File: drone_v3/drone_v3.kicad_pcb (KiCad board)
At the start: 2 copper layers, 47.5 x 47.5 mm, 94 parts, among them J1 USB_B_Micro, J14 Conn_01x02_Male, J19 Micro_SD_Card, J2 Conn_01x10_Female, J7 Conn_01x04_Male, J9 Conn_01x06_Male, Q1 2N3904, Q2 2N3904, U3 MPU-9250, U7 BMP388, U9 MCP1700-3302E_SOT23, Y1 Crystal_GND24

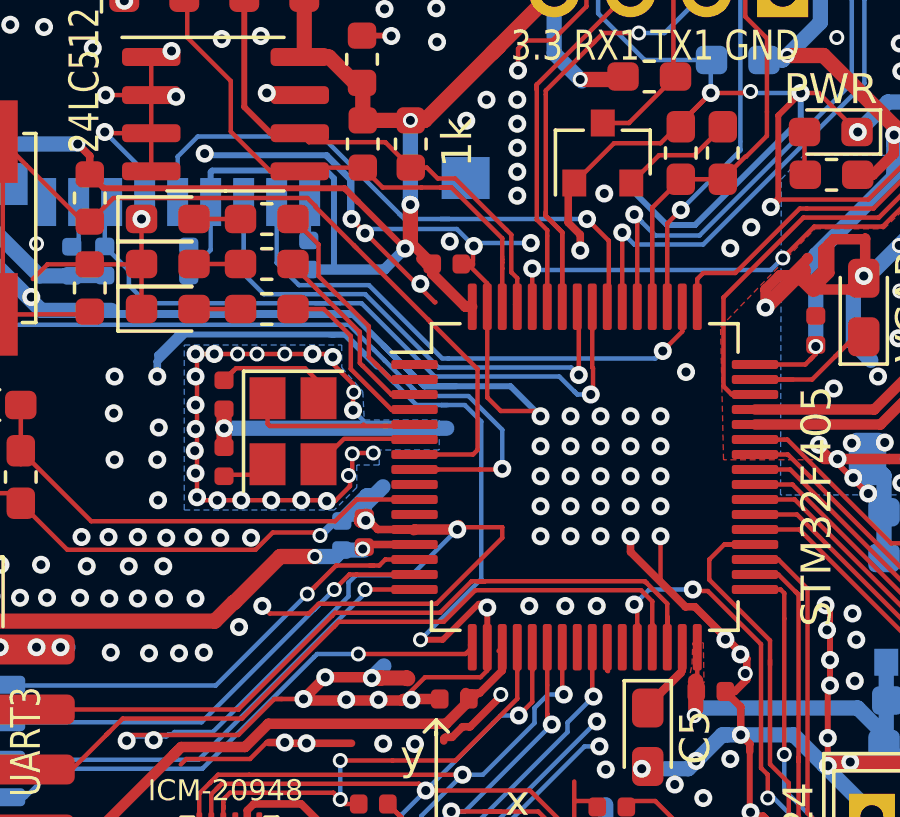
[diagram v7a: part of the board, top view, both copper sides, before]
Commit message: clearance to 0.2
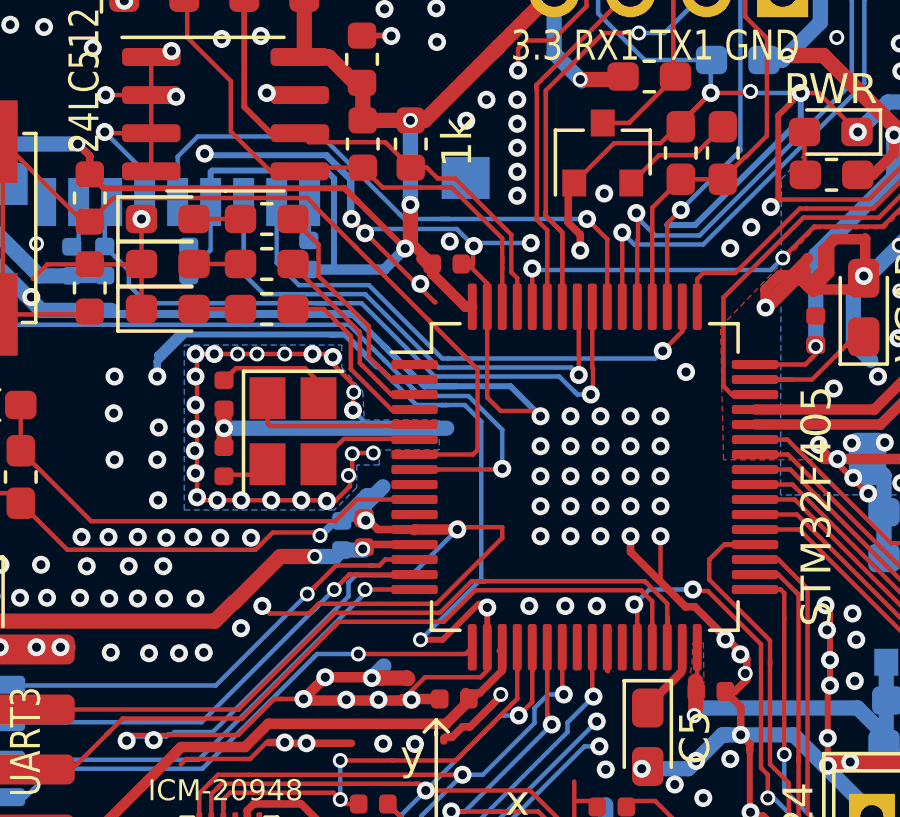
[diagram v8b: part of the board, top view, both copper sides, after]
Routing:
- net GND: track 657.6 -> 655.6 mm
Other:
- net class Default: clearance 0.15 -> 0.2
- rule trace_clearance: 0.15 -> 0.2
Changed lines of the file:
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@@
     (thickness 1.6)
     (drawings 10)
-    (tracks 1967)
+    (tracks 1968)
     (zones 0)
     (modules 94)
@@
     (user_trace_width 0.508)
     (user_trace_width 1.5)
-    (trace_clearance 0.15)
+    (trace_clearance 0.2)
     (zone_clearance 0.2)
     (zone_45_only no)
@@
   (net 103 PWR_IN)
   (net_class Default "This is the default net class."
-    (clearance 0.15)
+    (clearance 0.2)
     (trace_width 0.15)
     (via_dia 0.6)
@@
   (segment (start 128.125 124.65) (end 128.175 124.65) (width 0.15) (layer F.Cu) (net 1))
   (via (at 118.85 110.3) (size 0.6) (drill 0.3) (layers F.Cu B.Cu) (net 1))
-  (via (at 118.075 111) (size 0.6) (drill 0.3) (layers F.Cu B.Cu) (net 1))
+  (via (at 118.14 111.04) (size 0.6) (drill 0.3) (layers F.Cu B.Cu) (net 1))
   (segment (start 122.41651 97.73349) (end 122.275 97.875) (width 0.15) (layer B.Cu) (net 1))
   (segment (start 125.33349 97.73349) (end 122.41651 97.73349) (width 0.15) (layer B.Cu) (net 1))
@@
   (segment (start 129.45 98.45) (end 129.45 97.922816) (width 0.254) (layer F.Cu) (net 1))
   (segment (start 132.340003 97.600001) (end 133.274999 97.600001) (width 0.2) (layer B.Cu) (net 1))
-  (segment (start 130.940002 96.2) (end 132.340003 97.600001) (width 0.2) (layer B.Cu) (net 1))
   (segment (start 136.8 94.075) (end 136.8 93.2) (width 0.2) (layer B.Cu) (net 1))
   (segment (start 133.274999 97.600001) (end 136.8 94.075) (width 0.2) (layer B.Cu) (net 1))
@@
   (segment (start 144.268797 89.726201) (end 144.326201 89.726201) (width 0.15) (layer F.Cu) (net 31))
   (segment (start 141.44759 92.547408) (end 144.268797 89.726201) (width 0.15) (layer F.Cu) (net 31))
-  (segment (start 130.85 100.325) (end 130.85 97.85) (width 0.15) (layer F.Cu) (net 32))
   (segment (start 130.85 97.85) (end 130.85 97.85) (width 0.15) (layer F.Cu) (net 32))
   (via (at 130.85 97.85) (size 0.6) (drill 0.3) (layers F.Cu B.Cu) (net 32))
@@
   (segment (start 138.92 90.08) (end 141.58 87.42) (width 0.15) (layer B.Cu) (net 32))
   (segment (start 138.92 92.876998) (end 138.92 90.08) (width 0.15) (layer B.Cu) (net 32))
-  (segment (start 131.35 100.325) (end 131.35 97.35) (width 0.15) (layer F.Cu) (net 33))
-  (segment (start 131.35 97.35) (end 131.25 97.25) (width 0.15) (layer F.Cu) (net 33))
   (segment (start 131.25 97.25) (end 131.25 97.25) (width 0.15) (layer F.Cu) (net 33))
-  (via (at 131.25 97.25) (size 0.6) (drill 0.3) (layers F.Cu B.Cu) (net 33) (status 1000000))
+  (via (at 131.32 97.2) (size 0.6) (drill 0.3) (layers F.Cu B.Cu) (net 33))
   (segment (start 131.25 97.25) (end 131.5 97.5) (width 0.15) (layer B.Cu) (net 33))
   (segment (start 140.75 85.96) (end 140.75 87.825722) (width 0.15) (layer B.Cu) (net 33))
@@
   (segment (start 123.589088 97.4) (end 123.65 97.4) (width 0.15) (layer B.Cu) (net 50))
   (segment (start 124.8 97.4) (end 123.65 97.4) (width 0.15) (layer B.Cu) (net 50))
-  (segment (start 130.4 98.125) (end 129.675 97.4) (width 0.15) (layer F.Cu) (net 50))
   (segment (start 130.35 100.325) (end 130.4 100.275) (width 0.15) (layer F.Cu) (net 50))
-  (segment (start 130.4 100.275) (end 130.4 98.125) (width 0.15) (layer F.Cu) (net 50))
   (segment (start 129.2 97.4) (end 124.8 97.4) (width 0.15) (layer B.Cu) (net 50))
   (segment (start 129.675 97.4) (end 129.2 97.4) (width 0.15) (layer B.Cu) (net 50))
@@
   (segment (start 128.85 100.325) (end 128.85 97.85) (width 0.15) (layer F.Cu) (net 28))
   (segment (start 128.85 97.85) (end 128.3 97.3) (width 0.15) (layer F.Cu) (net 28))
+  (segment (start 130.85 100.325) (end 130.85 97.85) (width 0.15) (layer F.Cu) (net 32))
+  (segment (start 131.375001 98.102001) (end 131.375001 97.375001) (width 0.15) (layer F.Cu) (net 33))
+  (segment (start 131.375001 97.375001) (end 131.25 97.25) (width 0.15) (layer F.Cu) (net 33))
+  (segment (start 131.35 98.127002) (end 131.375001 98.102001) (width 0.15) (layer F.Cu) (net 33))
+  (segment (start 131.35 100.325) (end 131.35 98.127002) (width 0.15) (layer F.Cu) (net 33))
   (segment (start 123.419544 97.230456) (end 123.5 97.310912) (width 0.15) (layer B.Cu) (net 50))
   (segment (start 123.419544 97.230456) (end 123.589088 97.4) (width 0.15) (layer B.Cu) (net 50))
   (segment (start 120.839088 94.65) (end 123.419544 97.230456) (width 0.15) (layer B.Cu) (net 50))
+  (segment (start 130.35 98.075) (end 129.675 97.4) (width 0.15) (layer F.Cu) (net 50))
+  (segment (start 130.35 100.325) (end 130.35 98.075) (width 0.15) (layer F.Cu) (net 50))
   (segment (start 127.15121 97.922842) (end 126.989184 97.760816) (width 0.15) (layer F.Cu) (net 63))
   (segment (start 127.15121 99.174765) (end 127.15121 97.922842) (width 0.15) (layer F.Cu) (net 63))
